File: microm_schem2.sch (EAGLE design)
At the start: 81 parts, among them Q1 16 MHz

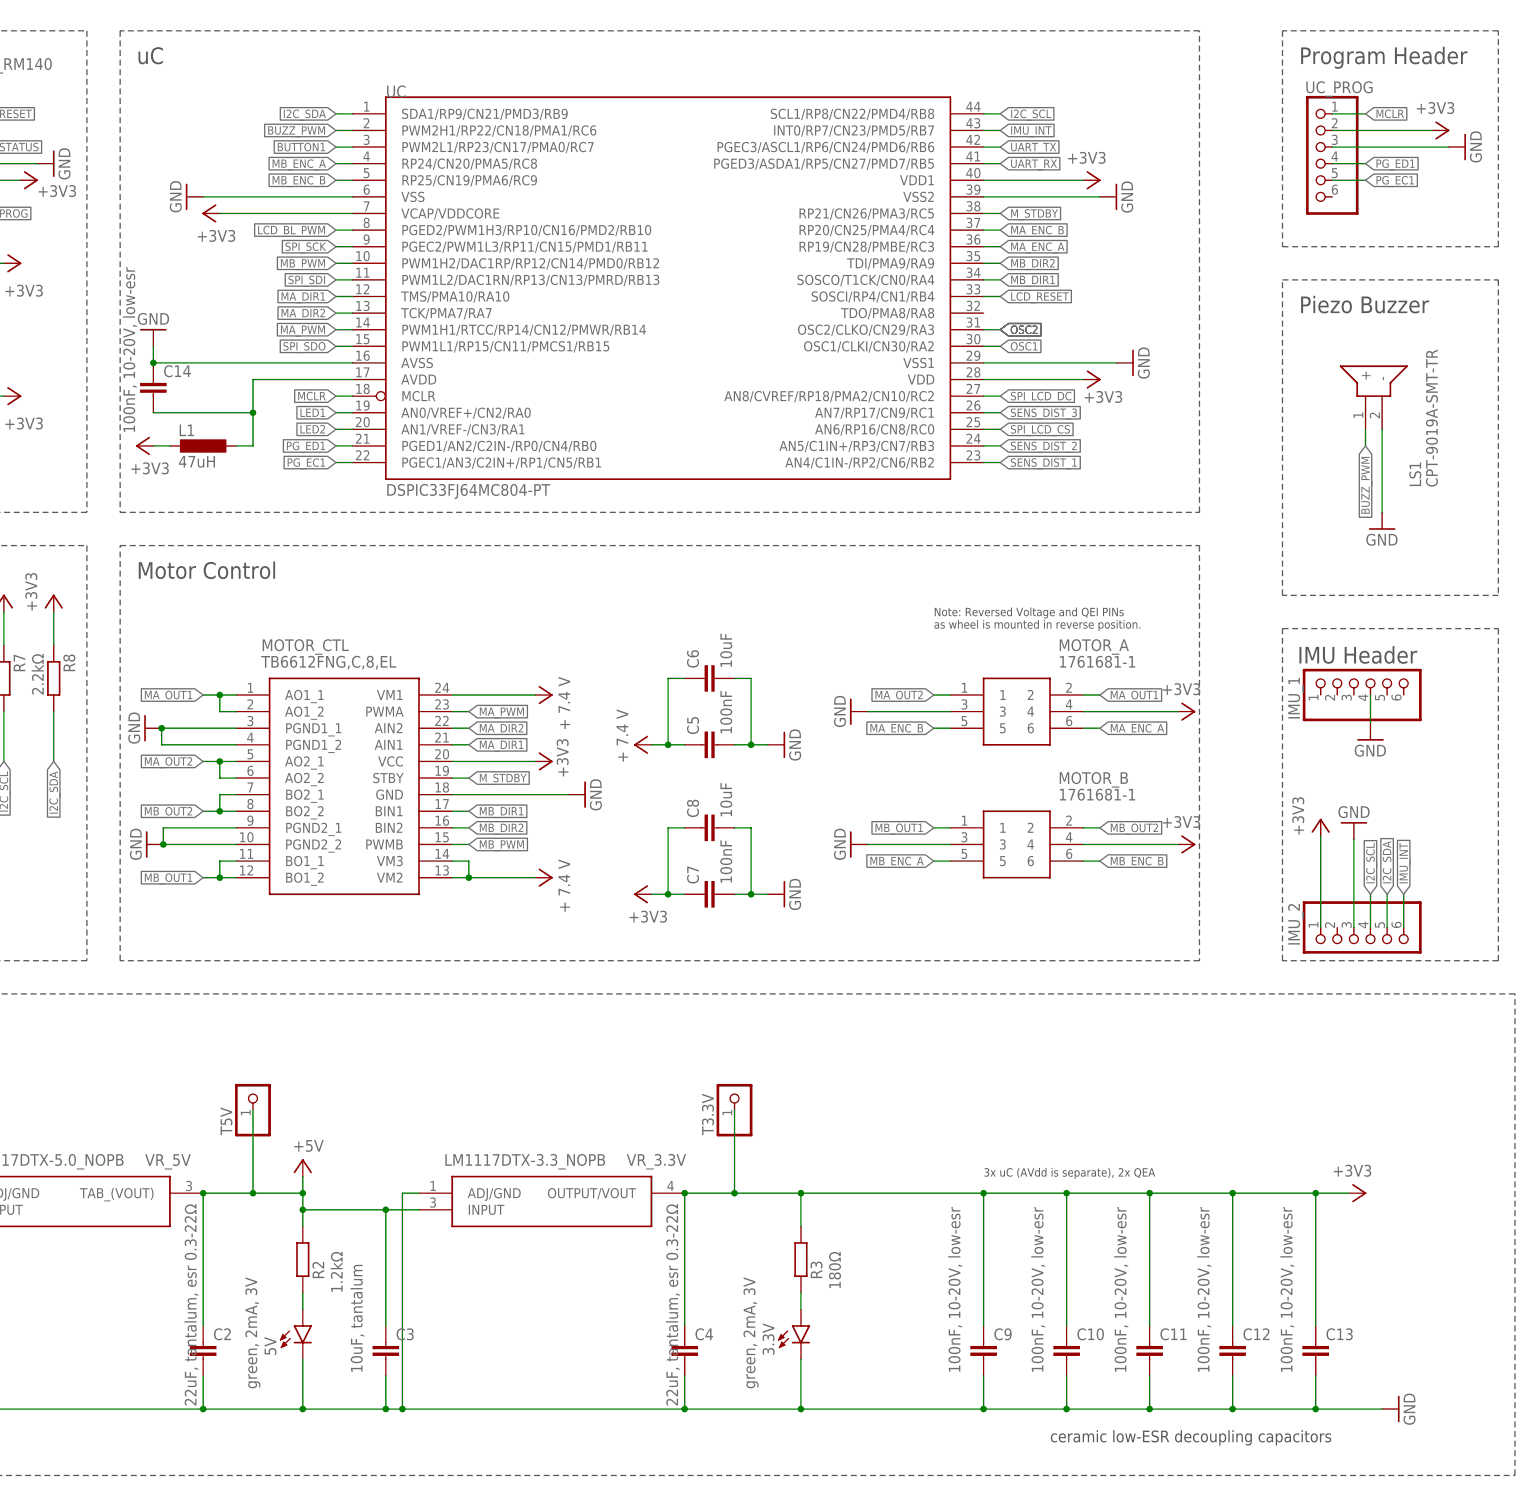
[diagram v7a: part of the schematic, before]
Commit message: WIP: Trace the airwires
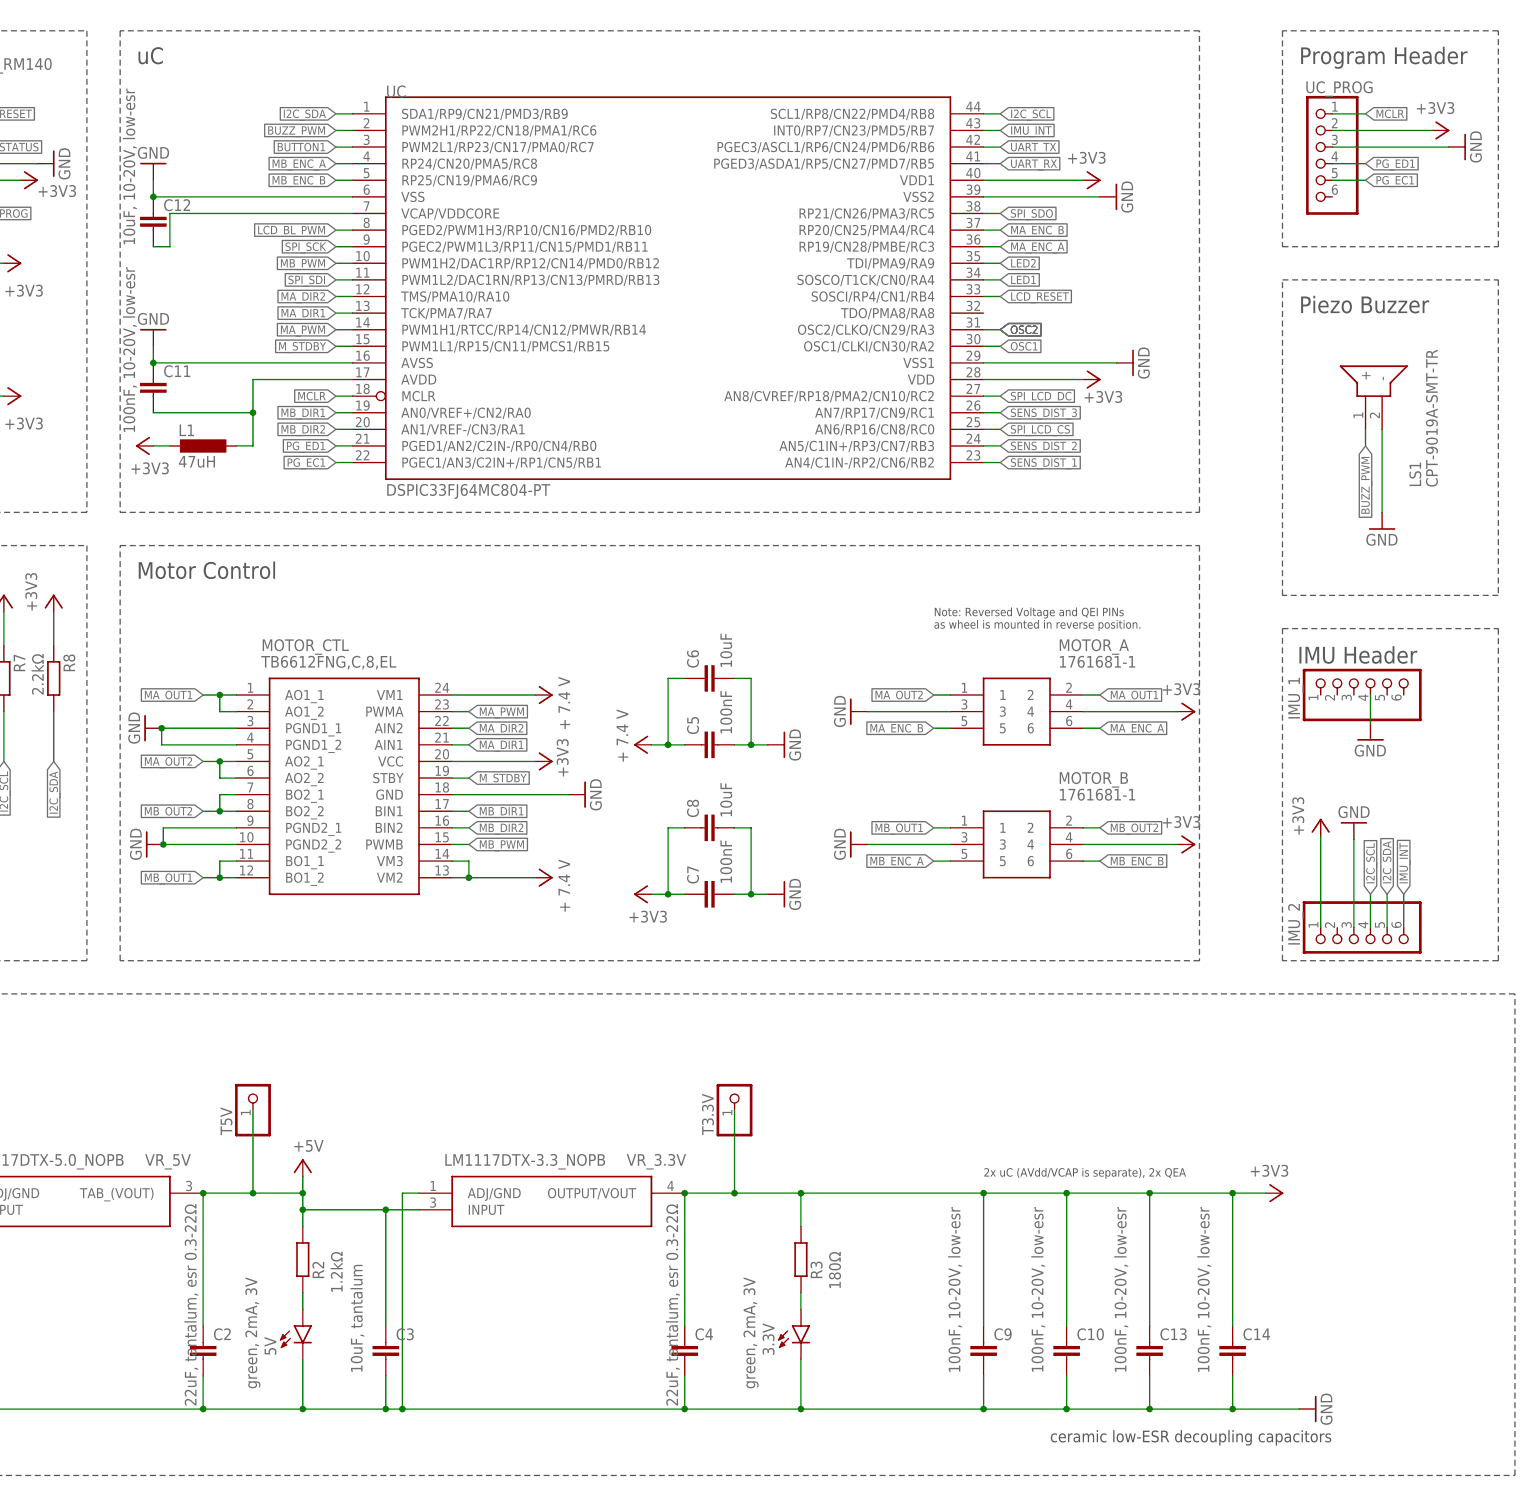
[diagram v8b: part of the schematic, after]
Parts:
- C12: value 100nF, 10-20V, low-esr -> 10uF, 10-20V, low-esr
- UC_PROG: device pinhead:PINHD-1X6/90 -> pinhead:PINHD-1X6
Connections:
- new net VCAP/VDDCORE: C12.2, UC.VCAP/VDDCORE
- net +3V3: now also C14.1; no longer C11.1, C12.1, UC.VCAP/VDDCORE
- net GND: now also C11.1, C12.1, C14.2; no longer C11.2, C12.2, C14.1
- net LED1: now also UC.SOSCO/T1CK/CN0/RA4; no longer UC.AN0/VREF+/CN2/RA0
- net LED2: now also UC.TDI/PMA9/RA9; no longer UC.AN1/VREF-/CN3/RA1
- net MA_DIR1: now also UC.TCK/PMA7/RA7; no longer UC.TMS/PMA10/RA10
- net MA_DIR2: now also UC.TMS/PMA10/RA10; no longer UC.TCK/PMA7/RA7
- net MB_DIR1: now also UC.AN0/VREF+/CN2/RA0; no longer UC.SOSCO/T1CK/CN0/RA4
- net MB_DIR2: now also UC.AN1/VREF-/CN3/RA1; no longer UC.TDI/PMA9/RA9
- net M_STDBY: now also UC.PWM1L1/RP15/CN11/PMCS1/RB15; no longer UC.RP21/CN26/PMA3/RC5
- net N$5: now also C11.2; no longer C14.2
- net SPI_SDO: now also UC.RP21/CN26/PMA3/RC5; no longer UC.PWM1L1/RP15/CN11/PMCS1/RB15
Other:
- note added: "2x uC (AVdd/VCAP is separate), 2x QEA"
- note removed: "3x uC (AVdd is separate), 2x QEA"
- moved on the sheet: C11, C12, C13, C14
